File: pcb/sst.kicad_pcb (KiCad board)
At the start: 2 copper layers, 90 x 90 mm, 40 parts, among them X1 CONN_SPI, X2 CONN_PWR, X3 CONN_INPUTS, X4 CONN_I2C, X5 CONN_INPUTS

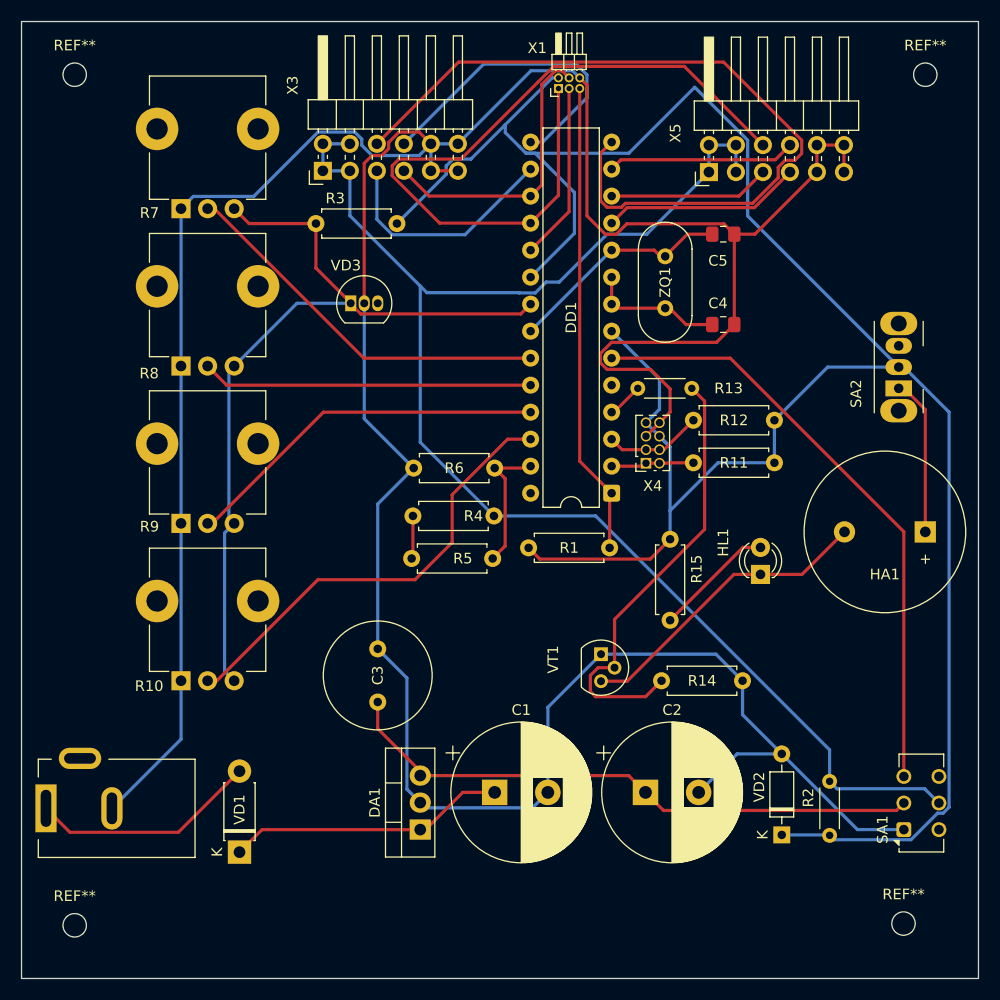
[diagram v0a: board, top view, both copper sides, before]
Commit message: размер платы 80x90mm
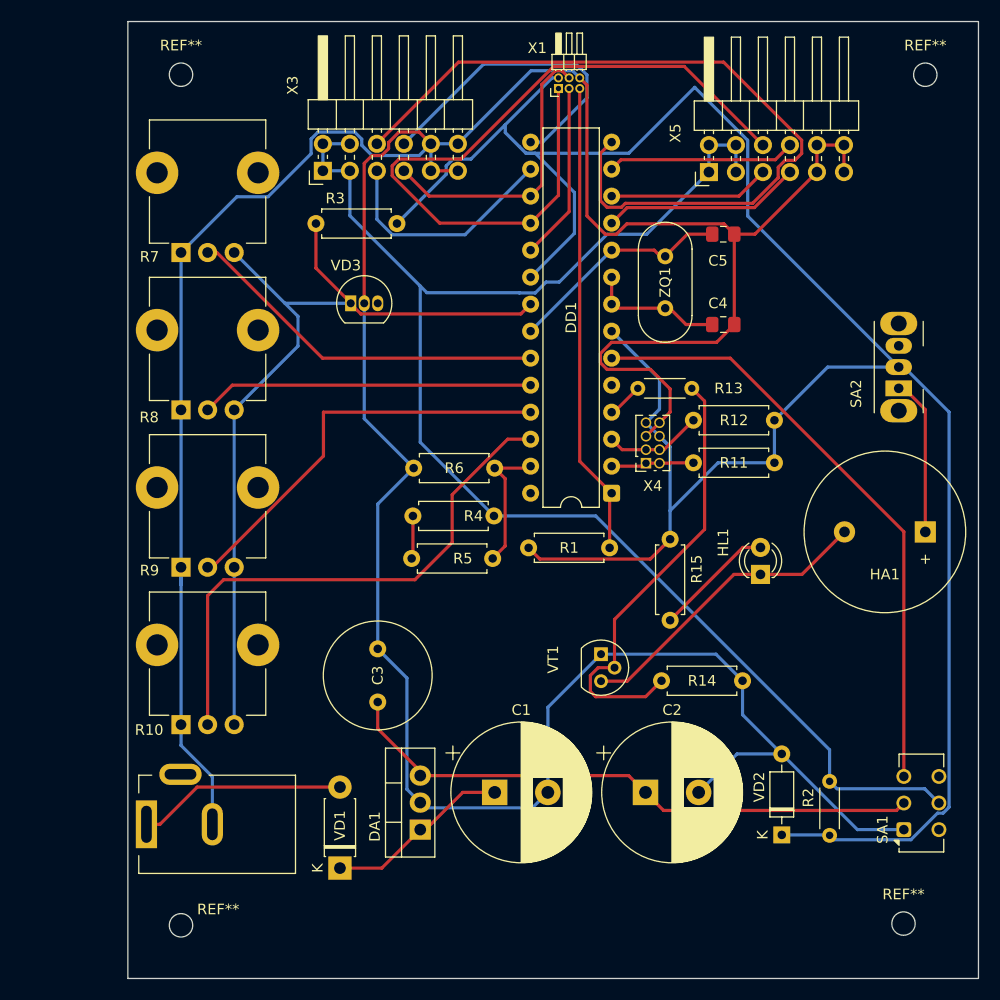
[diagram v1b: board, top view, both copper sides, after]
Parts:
- moved REF** 10.0 mm to (124.8, 100.2)
- moved REF** 10.0 mm to (124.8, 180.2)
- moved VD1 9.57 mm to (139.7, 174.8)
- moved X2 9.57 mm to (121.5, 170.7)
- moved R10 4.12 mm to (124.8, 161.3)
- moved R7 4.12 mm to (124.8, 116.9)
- moved R8 4.12 mm to (124.8, 131.7)
- moved R9 4.12 mm to (124.8, 146.5)
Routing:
- net Net-(DA1-VI): track 26.3 -> 17.5 mm
- net Net-(DD1-PC3): track 42.4 -> 51.2 mm
- net Net-(DD1-PC2): track 34.7 -> 38.8 mm
- net +2,5V: track 79.0 -> 82.2 mm
- net Net-(VD1-A): track 21.5 -> 19.6 mm
- net Net-(DD1-PC0): track 36.2 -> 34.5 mm
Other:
- board size 90 x 90 mm -> 80 x 90 mm
- board text added: "80.0000 mm x 90.0000 mm"
- board text removed: "90.0000 mm x 90.0000 mm"

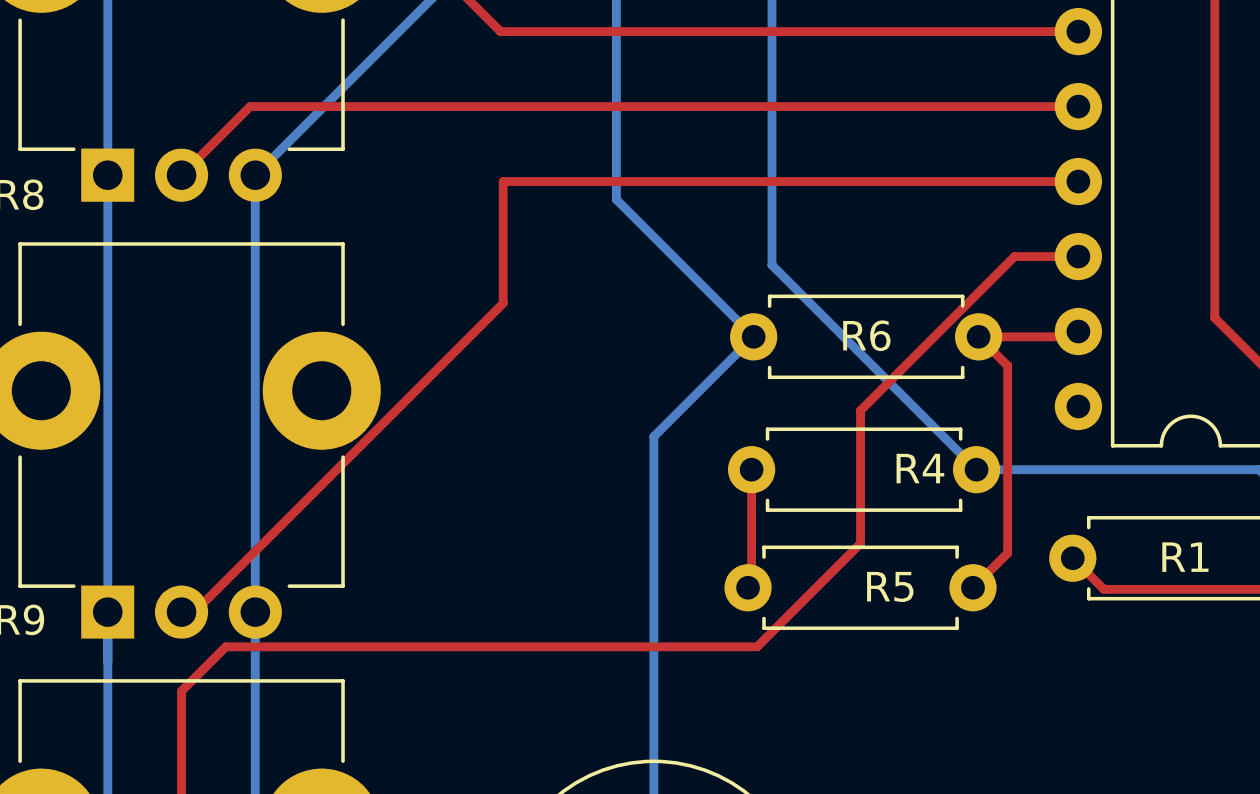
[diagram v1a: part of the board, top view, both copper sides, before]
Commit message: убрал проводник с углом под 90 градусов
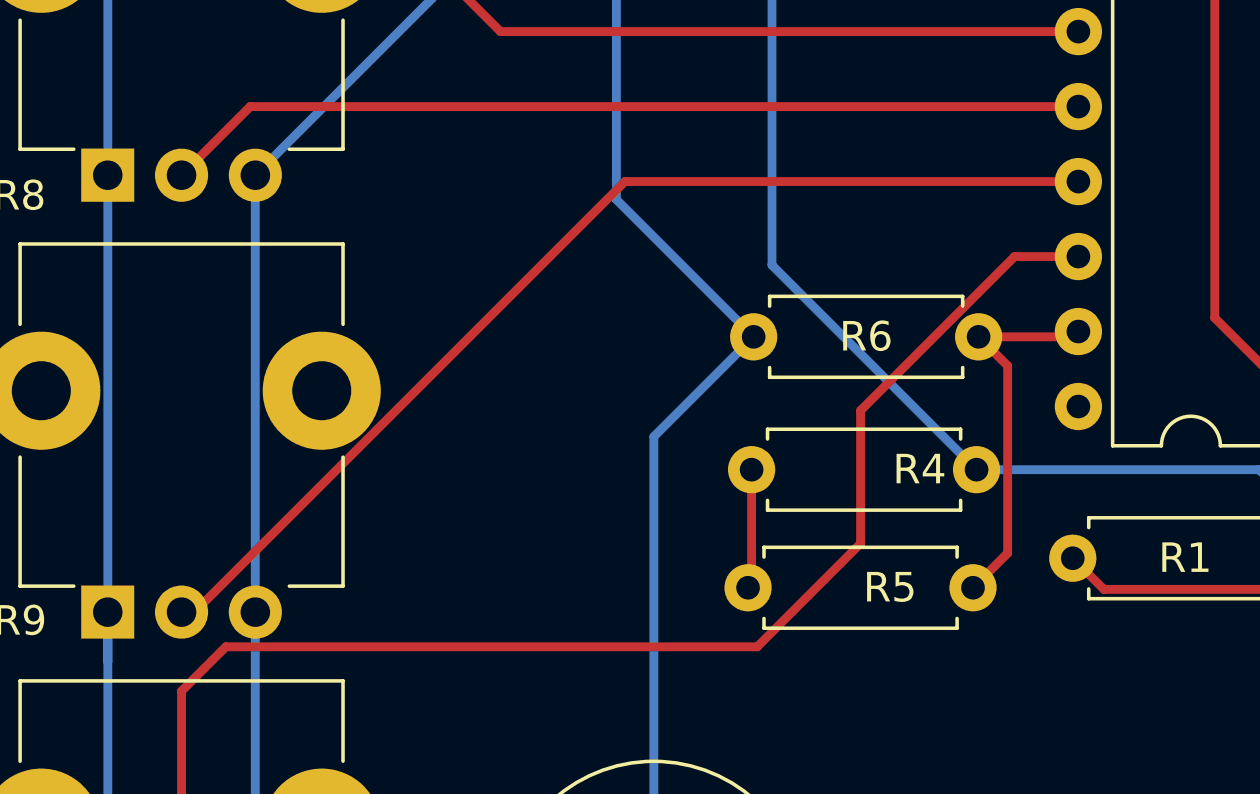
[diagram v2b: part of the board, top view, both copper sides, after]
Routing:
- net Net-(DD1-PC2): track 38.8 -> 36.4 mm
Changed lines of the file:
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@@
 	)
 	(segment
-		(start 138.151258 131.9044)
+		(start 142.276258 131.9044)
 		(end 157.6356 131.9044)
 		(width 0.3)
@@
 	)
 	(segment
-		(start 138.151258 136.0294)
+		(start 127.2556 146.4894)
 		(end 127.691258 146.4894)
 		(width 0.3)
@@
 	)
 	(segment
-		(start 138.151258 131.9044)
-		(end 138.151258 136.0294)
+		(start 127.691258 146.4894)
+		(end 142.276258 131.9044)
 		(width 0.3)
 		(layer "F.Cu")
-		(net 21)
-	)
-	(segment
-		(start 127.691258 146.4894)
-		(end 127.2556 146.4894)
-		(width 0.3)
-		(layer "F.Cu")
